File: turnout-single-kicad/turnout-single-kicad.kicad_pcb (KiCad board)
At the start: 2 copper layers, 38.5 x 15 mm, 14 parts, among them SW1 SW_Push_DPDT

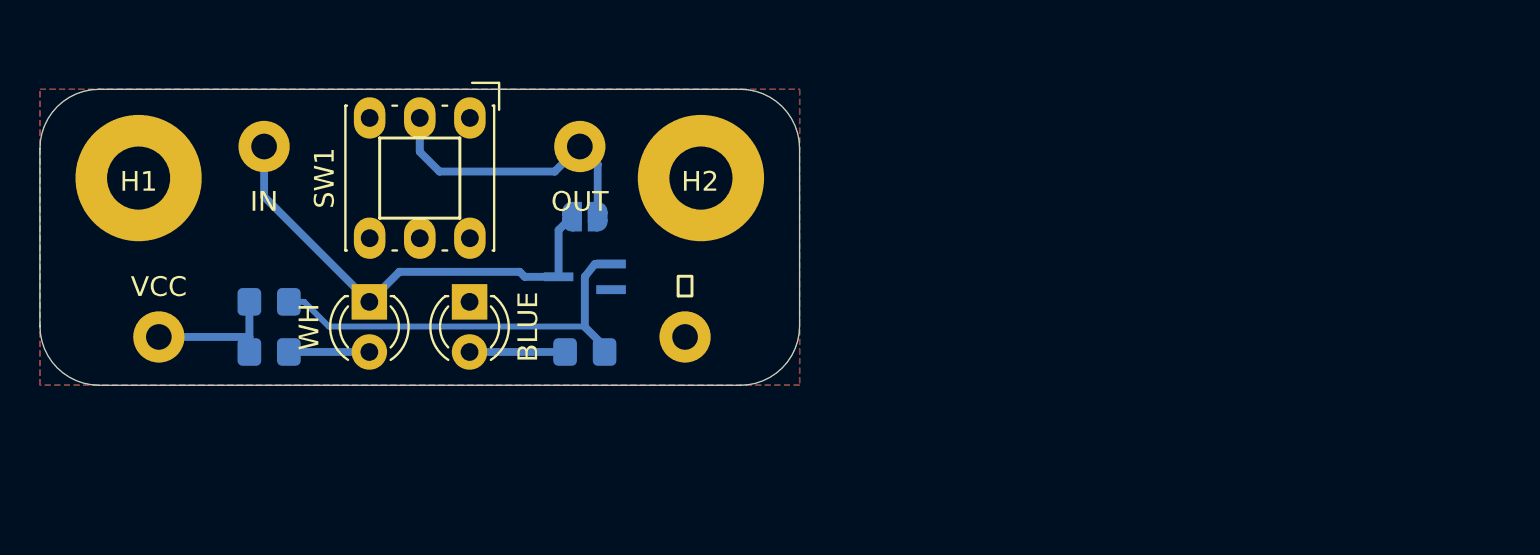
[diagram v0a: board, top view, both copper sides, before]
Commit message: Add turnout-single pcb.
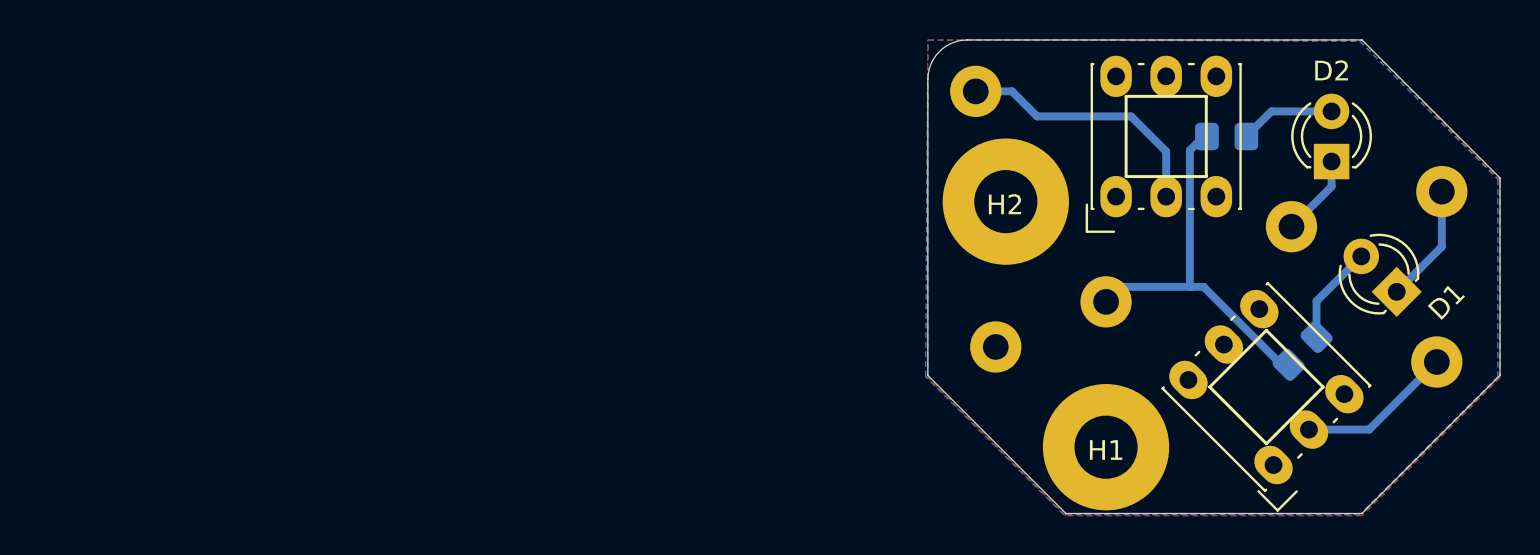
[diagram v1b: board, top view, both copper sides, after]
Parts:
- removed BLUE: STOP, LED_THT:LED_D3.0mm
- removed JP1: SolderJumper_2_Open, Jumper:SolderJumper-2_P1.3mm_Open_RoundedPad1.0x1.5mm
- removed R3: 1k, Resistor_SMD:R_0805_2012Metric_Pad1.20x1.40mm_HandSolder
- removed ⏚: pad, Connector_Pin:Pin_D1.3mm_L11.0mm
- added -: SW_Push_DPDT, Switch_KMZ:KLS7, F.Cu at (137.2, 37.6)
- added BTN-: pad, Connector_Pin:Pin_D1.3mm_L11.0mm, B.Cu at (145.8, 36.3)
- added GND: pad, Connector_Pin:Pin_D1.3mm_L11.0mm, B.Cu at (123.4, 35.6)
- added LED+: pad, Connector_Pin:Pin_D1.3mm_L11.0mm, B.Cu at (138.4, 29.5)
- D1: renamed from WH; value GO -> PLUS
- D2: value BAT54W -> MINUS; footprint Package_TO_SOT_SMD:SOT-323_SC-70_Handsoldering -> LED_THT:LED_D3.0mm; moved to F.Cu
- moved LED- 59.7 mm to (146.1, 27.7)
- moved R1 52.4 mm to (139.0, 35.8), turned to 45 degrees
- moved D1 52.1 mm to (143.8, 32.8), turned to 135 degrees
- moved H1 50.9 mm to (129.0, 40.6)
- moved R2 49.2 mm to (135.1, 24.9)
- moved VCC 48.0 mm to (129.0, 33.3)
- moved D2 38.3 mm to (140.5, 26.2), turned to 90 degrees
- moved + 37.9 mm to (132.1, 24.9), turned to 90 degrees
- moved BTN+ 20.3 mm to (122.4, 22.6)
- moved H2 15.5 mm to (124.0, 28.2)
- renumbered SW1 to +, OUT to BTN+, IN to LED-
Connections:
- D1 pad 1: Net-(CINPUT1-Pad1) -> Net-(D1-Pad1)
- D2 pad 2: (no net) -> Net-(D2-Pad2)
- LED- pad 1: Net-(CINPUT1-Pad1) -> Net-(D1-Pad1)
- R2 pad 2: Net-(D2-Pad1) -> Net-(D2-Pad2)
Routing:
- net Net-(CINPUT1-Pad1): track 23.7 -> 0.00 mm
- net Net-(D2-Pad1): track 21.4 -> 4.14 mm
- net VCC: track 7.13 -> 19.2 mm
- net Net-(OMINUS1-Pad1): track 0.00 -> 7.90 mm
- net Net-(D1-Pad1): track 0.00 -> 6.03 mm
- net Net-(D2-Pad2): track 0.00 -> 4.84 mm
- net Net-(D3-Pad2): track 4.84 -> 0.00 mm
- net Net-(OPLUS1-Pad1): track 16.0 -> 13.2 mm
- net Net-(D1-Pad2): track 4.08 -> 5.02 mm
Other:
- board size 38.5 x 15 mm -> 29 x 24 mm
- board text removed: "IN"
- board text removed: "Návěstidlo Se v1.0 JH 2021"
- board text removed: "OUT"
- board text removed: "VCC"
- board text removed: "⏚"

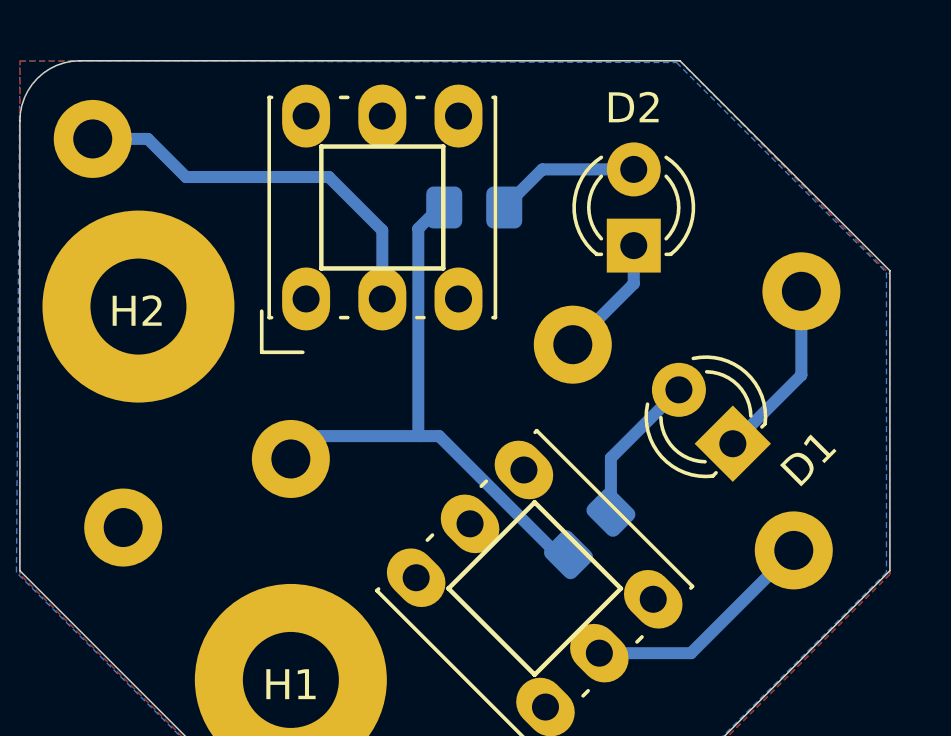
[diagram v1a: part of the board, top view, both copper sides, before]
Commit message: Add solder-jumpers for connecting inputs & outputs.
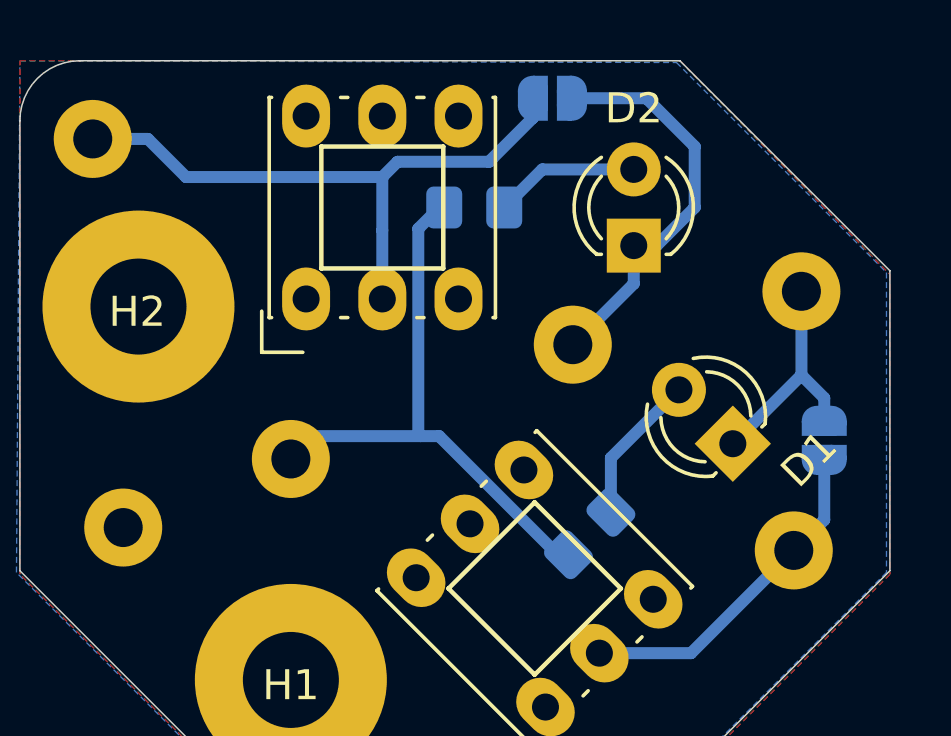
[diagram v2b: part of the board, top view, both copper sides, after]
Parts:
- added JP1: SJ, Jumper:SolderJumper-2_P1.3mm_Open_RoundedPad1.0x1.5mm, B.Cu at (137.8, 21.2)
- added JP2: SJ, Jumper:SolderJumper-2_P1.3mm_Open_RoundedPad1.0x1.5mm, B.Cu at (146.8, 32.7)
- renumbered R2 to R+, R1 to R-
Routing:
- net Net-(D2-Pad1): track 4.14 -> 13.5 mm
- net Net-(JP1-Pad2): track 13.2 -> 20.7 mm
- net Net-(JP2-Pad2): track 7.90 -> 11.3 mm
- net Net-(D1-Pad1): track 6.03 -> 7.87 mm

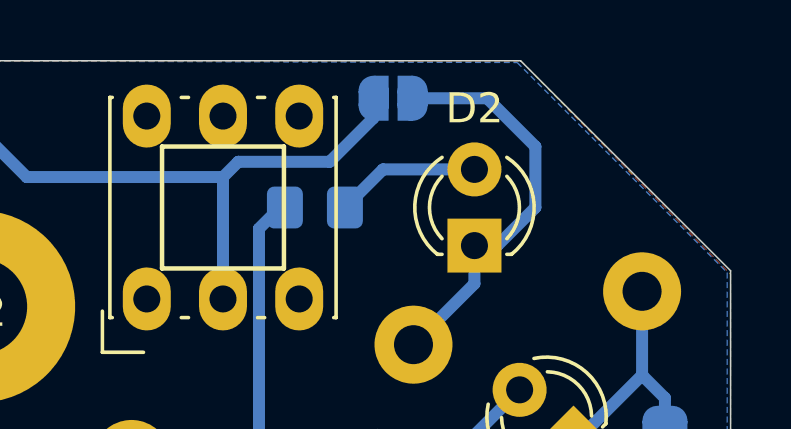
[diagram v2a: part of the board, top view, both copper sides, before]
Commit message: Add description as plain texts.
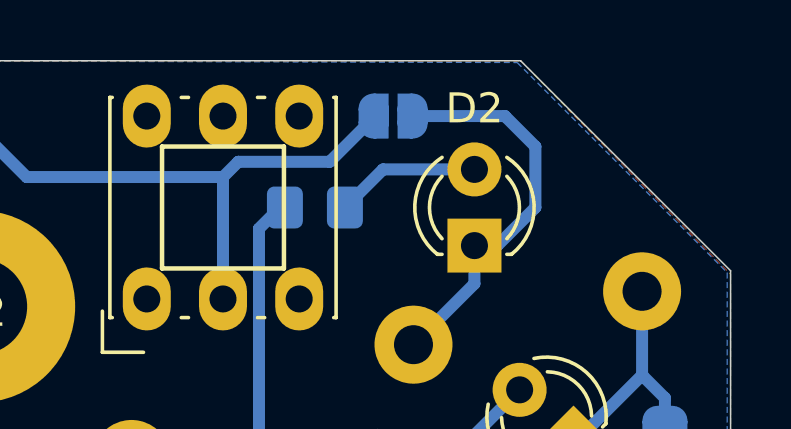
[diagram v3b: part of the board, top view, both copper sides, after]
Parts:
- moved JP1 0.59 mm to (137.8, 21.8)
- renumbered GND to GND1, LED+ to IMINUS1, LED- to IPLUS1, BTN- to OMINUS1, BTN+ to OPLUS1, R- to R1, R+ to R2, - to SWMINUS1, + to SWPLUS1, VCC to VCC1
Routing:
- net Net-(JP1-Pad2): track 20.7 -> 20.1 mm
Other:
- board text added: "+"
- board text added: "-"
- board text added: "BTN+"
- board text added: "BTN-"
- board text added: "GND"
- board text added: "LED+"
- board text added: "LED-"
- board text added: "VCC"
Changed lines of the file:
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@@
   (general
     (thickness 1.6)
-    (drawings 816)
-    (tracks 37)
+    (drawings 824)
+    (tracks 36)
     (zones 0)
     (modules 16)
@@
   )
   (module Jumper:SolderJumper-2_P1.3mm_Open_RoundedPad1.0x1.5mm (layer B.Cu)
-    (at 137.75 21.25 180)
+    (at 137.75 21.844 180)
     (descr "SMD Solder Jumper, 1x1.5mm, rounded Pads, 0.3mm gap, open")
     (tags "solder jumper open")
@@
     (descr "solder Pin_ diameter 1.3mm, hole diameter 1.3mm, length 11.0mm")
     (tags "solder Pin_ pressfit")
-    (fp_text reference VCC (at 0 2.794) (layer B.SilkS)
+    (fp_text reference VCC1 (at 0 2.794) (layer B.SilkS) hide
       (effects (font (size 1 1) (thickness 0.15)) (justify mirror))
     )
@@
     (descr "solder Pin_ diameter 1.3mm, hole diameter 1.3mm, length 11.0mm")
     (tags "solder Pin_ pressfit")
-    (fp_text reference GND (at 0 -2.54) (layer B.SilkS)
+    (fp_text reference GND1 (at 0 -2.54) (layer B.SilkS) hide
       (effects (font (size 1 1) (thickness 0.15)) (justify mirror))
     )
@@
   (module Switch_KMZ:KLS7 (layer F.Cu)
     (at 137.16 37.592 135)
-    (fp_text reference - (at 0 0 225) (layer B.SilkS)
+    (fp_text reference SWMINUS1 (at 0 0 225) (layer B.SilkS) hide
       (effects (font (size 2 2) (thickness 0.15)) (justify mirror))
     )
@@
     (tags "resistor handsolder")
     (attr smd)
-    (fp_text reference R+ (at 1.856 1.778) (layer B.SilkS)
+    (fp_text reference R2 (at 1.856 1.778) (layer B.SilkS)
       (effects (font (size 1 1) (thickness 0.15)) (justify mirror))
     )
@@
     (descr "solder Pin_ diameter 1.3mm, hole diameter 1.3mm, length 11.0mm")
     (tags "solder Pin_ pressfit")
-    (fp_text reference BTN- (at -2.546 3.428 45) (layer B.SilkS)
+    (fp_text reference OMINUS1 (at -2.546 3.428 45) (layer B.SilkS) hide
       (effects (font (size 1 1) (thickness 0.15)) (justify mirror))
     )
@@
     (descr "solder Pin_ diameter 1.3mm, hole diameter 1.3mm, length 11.0mm")
     (tags "solder Pin_ pressfit")
-    (fp_text reference LED+ (at -3.68 1.036) (layer B.SilkS)
+    (fp_text reference IMINUS1 (at -3.68 1.036) (layer B.SilkS) hide
       (effects (font (size 1 1) (thickness 0.15)) (justify mirror))
     )
@@
     (descr "solder Pin_ diameter 1.3mm, hole diameter 1.3mm, length 11.0mm")
     (tags "solder Pin_ pressfit")
-    (fp_text reference BTN+ (at 3.822 -0.106) (layer B.SilkS)
+    (fp_text reference OPLUS1 (at 3.822 -0.106) (layer B.SilkS) hide
       (effects (font (size 1 1) (thickness 0.15)) (justify mirror))
     )
@@
     (descr "solder Pin_ diameter 1.3mm, hole diameter 1.3mm, length 11.0mm")
     (tags "solder Pin_ pressfit")
-    (fp_text reference LED- (at -2.794 -0.508 -90) (layer B.SilkS)
+    (fp_text reference IPLUS1 (at -2.794 -0.508 -90) (layer B.SilkS) hide
       (effects (font (size 1 1) (thickness 0.15)) (justify mirror))
     )
@@
   (module Switch_KMZ:KLS7 (layer F.Cu)
     (at 132.08 24.892 90)
-    (fp_text reference + (at 0 0 90) (layer B.SilkS)
+    (fp_text reference SWPLUS1 (at 0 0 90) (layer B.SilkS) hide
       (effects (font (size 2 2) (thickness 0.15)) (justify mirror))
     )
@@
     (tags "resistor handsolder")
     (attr smd)
-    (fp_text reference R- (at 2.839892 -0.001414 45) (layer B.SilkS)
+    (fp_text reference R1 (at 2.839892 -0.001414 45) (layer B.SilkS)
       (effects (font (size 1 1) (thickness 0.15)) (justify mirror))
     )
@@
       (rotate (xyz 0 0 0))
     )
+  )
+  (gr_text - (at 137.16 37.592 45) (layer B.SilkS)
+    (effects (font (size 2 2) (thickness 0.15)) (justify mirror))
+  )
+  (gr_text + (at 132.08 24.892) (layer B.SilkS)
+    (effects (font (size 2 2) (thickness 0.15)) (justify mirror))
+  )
+  (gr_text LED- (at 143.256 27.178 270) (layer B.SilkS)
+    (effects (font (size 1 1) (thickness 0.15)) (justify mirror))
+  )
+  (gr_text BTN- (at 143.256 39.878 45) (layer B.SilkS)
+    (effects (font (size 1 1) (thickness 0.15)) (justify mirror))
+  )
+  (gr_text LED+ (at 134.62 30.48) (layer B.SilkS)
+    (effects (font (size 1 1) (thickness 0.15)) (justify mirror))
+  )
+  (gr_text VCC (at 129.032 36.068) (layer B.SilkS)
+    (effects (font (size 1 1) (thickness 0.15)) (justify mirror))
+  )
+  (gr_text GND (at 123.444 33.02) (layer B.SilkS)
+    (effects (font (size 1 1) (thickness 0.15)) (justify mirror))
+  )
+  (gr_text BTN+ (at 126.238 22.606) (layer B.SilkS)
+    (effects (font (size 1 1) (thickness 0.15)) (justify mirror))
   )
   (gr_arc (start 122 22) (end 122 20) (angle -90) (layer Edge.Cuts) (width 0.05))
@@
   (segment (start 140.462 27.432) (end 138.43 29.464) (width 0.4) (layer B.Cu) (net 6))
   (segment (start 140.462 26.162) (end 140.462 27.432) (width 0.4) (layer B.Cu) (net 6))
-  (segment (start 138.4 21.25) (end 140.884 21.25) (width 0.4) (layer B.Cu) (net 6))
-  (segment (start 140.884 21.25) (end 142.494 22.86) (width 0.4) (layer B.Cu) (net 6))
+  (segment (start 138.4 21.844) (end 141.478 21.844) (width 0.4) (layer B.Cu) (net 6))
+  (segment (start 141.478 21.844) (end 142.494 22.86) (width 0.4) (layer B.Cu) (net 6))
   (segment (start 142.494 22.86) (end 142.494 24.892) (width 0.4) (layer B.Cu) (net 6))
   (segment (start 141.224 26.162) (end 140.462 26.162) (width 0.4) (layer B.Cu) (net 6))
@@
   (segment (start 135.636 23.368) (end 132.588 23.368) (width 0.4) (layer B.Cu) (net 8))
   (segment (start 137.1 21.904) (end 135.636 23.368) (width 0.4) (layer B.Cu) (net 8))
-  (segment (start 137.1 21.25) (end 137.1 21.904) (width 0.4) (layer B.Cu) (net 8))
   (zone (net 1) (net_name GND) (layer B.Cu) (hatch edge 0.508)
     (connect_pads (clearance 0.4))

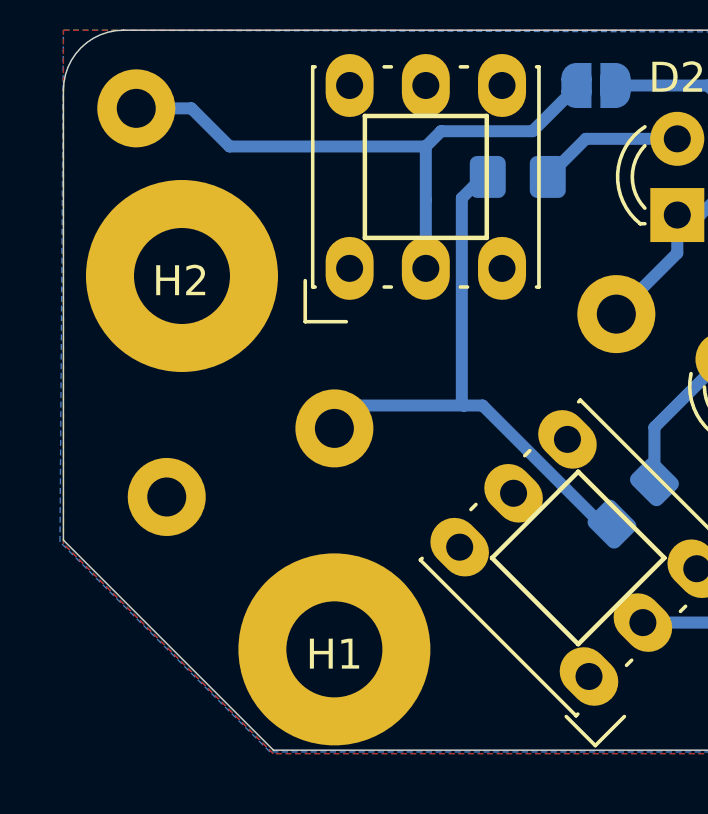
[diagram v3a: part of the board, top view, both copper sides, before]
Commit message: Remove Cu from around mounting holes.
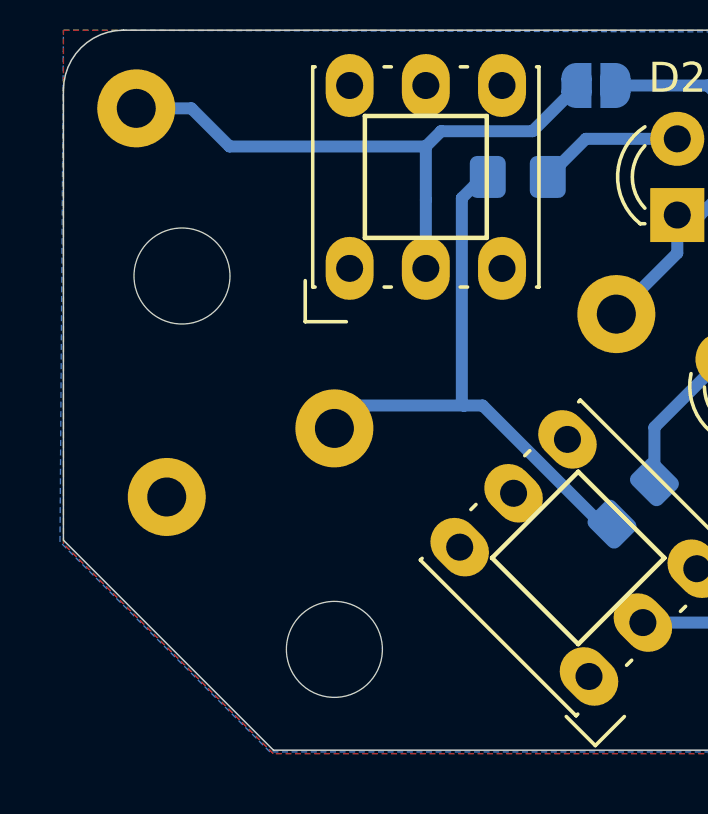
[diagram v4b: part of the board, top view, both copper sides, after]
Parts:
- H1, H2: footprint MountingHole:MountingHole_3.2mm_M3_Pad -> MountingHole:MountingHole_3.2mm_M3
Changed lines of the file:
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@@
     (add_net VCC)
+  )
+  (module MountingHole:MountingHole_3.2mm_M3 (layer F.Cu)
+    (at 123.952 28.194)
+    (descr "Mounting Hole 3.2mm, no annular, M3")
+    (tags "mounting hole 3.2mm no annular m3")
+    (attr virtual)
+    (fp_text reference H2 (at 0 -4.2) (layer F.SilkS) hide
+      (effects (font (size 1 1) (thickness 0.15)))
+    )
+    (fp_text value MountingHole (at 0 4.2) (layer F.Fab)
+      (effects (font (size 1 1) (thickness 0.15)))
+    )
+    (fp_text user %R (at 0.3 0) (layer F.Fab)
+      (effects (font (size 1 1) (thickness 0.15)))
+    )
+    (fp_circle (center 0 0) (end 3.2 0) (layer Cmts.User) (width 0.15))
+    (fp_circle (center 0 0) (end 3.45 0) (layer F.CrtYd) (width 0.05))
+    (pad 1 np_thru_hole circle (at 0 0) (size 3.2 3.2) (drill 3.2) (layers *.Cu *.Mask))
+  )
+  (module MountingHole:MountingHole_3.2mm_M3 (layer F.Cu)
+    (at 129.032 40.64)
+    (descr "Mounting Hole 3.2mm, no annular, M3")
+    (tags "mounting hole 3.2mm no annular m3")
+    (attr virtual)
+    (fp_text reference H1 (at 0 -4.2) (layer F.SilkS) hide
+      (effects (font (size 1 1) (thickness 0.15)))
+    )
+    (fp_text value MountingHole (at 0 4.2) (layer F.Fab)
+      (effects (font (size 1 1) (thickness 0.15)))
+    )
+    (fp_text user %R (at 0.3 0) (layer F.Fab)
+      (effects (font (size 1 1) (thickness 0.15)))
+    )
+    (fp_circle (center 0 0) (end 3.2 0) (layer Cmts.User) (width 0.15))
+    (fp_circle (center 0 0) (end 3.45 0) (layer F.CrtYd) (width 0.05))
+    (pad 1 np_thru_hole circle (at 0 0) (size 3.2 3.2) (drill 3.2) (layers *.Cu *.Mask))
   )
   (module Jumper:SolderJumper-2_P1.3mm_Open_RoundedPad1.0x1.5mm (layer B.Cu)
@@
     )
   )
-  (module MountingHole:MountingHole_3.2mm_M3_Pad (layer F.Cu)
-    (at 123.952 28.194)
-    (descr "Mounting Hole 3.2mm, M3")
-    (tags "mounting hole 3.2mm m3")
-    (attr virtual)
-    (fp_text reference H2 (at -0.042 0.178) (layer F.SilkS)
-      (effects (font (size 1 1) (thickness 0.15)))
-    )
-    (fp_text value MountingHole (at 0 4.2) (layer F.Fab)
-      (effects (font (size 1 1) (thickness 0.15)))
-    )
-    (fp_circle (center 0 0) (end 3.2 0) (layer Cmts.User) (width 0.15))
-    (fp_circle (center 0 0) (end 3.45 0) (layer F.CrtYd) (width 0.05))
-    (fp_text user %R (at 0.3 0) (layer F.Fab)
-      (effects (font (size 1 1) (thickness 0.15)))
-    )
-    (pad 1 thru_hole circle (at 0 0) (size 6.4 6.4) (drill 3.2) (layers *.Cu *.Mask))
-  )
-  (module MountingHole:MountingHole_3.2mm_M3_Pad (layer F.Cu)
-    (at 129.032 40.64)
-    (descr "Mounting Hole 3.2mm, M3")
-    (tags "mounting hole 3.2mm m3")
-    (attr virtual)
-    (fp_text reference H1 (at 0 0.178) (layer F.SilkS)
-      (effects (font (size 1 1) (thickness 0.15)))
-    )
-    (fp_text value MountingHole (at 0 4.2) (layer F.Fab)
-      (effects (font (size 1 1) (thickness 0.15)))
-    )
-    (fp_circle (center 0 0) (end 3.2 0) (layer Cmts.User) (width 0.15))
-    (fp_circle (center 0 0) (end 3.45 0) (layer F.CrtYd) (width 0.05))
-    (fp_text user %R (at 0.3 0) (layer F.Fab)
-      (effects (font (size 1 1) (thickness 0.15)))
-    )
-    (pad 1 thru_hole circle (at 0 0) (size 6.4 6.4) (drill 3.2) (layers *.Cu *.Mask))
-  )
   (module Switch_KMZ:KLS7 (layer F.Cu)
